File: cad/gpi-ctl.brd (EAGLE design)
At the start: 75 x 73.5 mm, 91 parts, among them CN2 MICROSDPLAIN, CN3 1X4-BIG, IC1 7803SR, SW1 SWITCHGT12-THOLE, SW2 SWITCHKMR211, SW3 SWITCHKMR211, U1 STM32F4/64, U2 ACS711, U3 ULN2003, U8 IC_FT230X-SSOP-16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

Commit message: regulator
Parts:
- removed IC1: 7803SR, adafruit:TO220H
- added C36: (no value), jaw:SMD0603
- added C37: 10u, jaw:SMD0603
- added J4: 1X4-BIG, adafruit:1X04-BIG
- added VREG1: ROF-78E3.3-0.5, jaw:ROF7800
- added VREG2: MCP1824, jaw:SOT-23-5
- moved C3 2.20 mm to (81.4, 29.2)
- moved C1 2.10 mm to (77.9, 29.2)
- moved C7 1.97 mm to (62.0, 59.7)
- moved C27 0.90 mm to (73.5, 62.2)
- moved D1 0.80 mm to (73.4, 60.3)
- moved NY1 0.80 mm to (72.2, 55.7)
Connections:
- new net N$8: D2.C, VREG2.1, VREG2.3
- net GND: now also C36.2, C37.2, J4.2, VREG1.2, VREG2.2; no longer IC1.2
- net I2CC: now also J4.4
- net I2CD: now also J4.3
- net VCC: now also C36.1, C37.1, J4.1, VREG1.3, VREG2.5; no longer IC1.3
- net VCCM: now also VREG1.1; no longer IC1.1
- net VIN: no longer D2.C
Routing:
- net VIN: track 40.8 -> 22.3 mm, vias 0 -> 1
- net N$8: track 0.00 -> 11.7 mm
- net GND: track 149.8 -> 159.6 mm, vias 94 -> 108
- net VCC: track 88.4 -> 96.2 mm, vias 17 -> 21
- net VBUS: track 20.6 -> 26.0 mm, vias 2 -> 3
- net I2CD: track 53.3 -> 58.4 mm, vias 0 -> 1
- net I2CC: track 57.9 -> 60.6 mm
- net VCCM: track 68.6 -> 70.5 mm
- net SPKR: track 35.8 -> 34.1 mm
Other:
- board text added: "C"
- board text added: "D"
- board text added: "T:BT0"
- board text added: "T:G"
- board text added: "T:Rx"
- board text added: "T:Tx"
- board text added: "T:Vi"
- board text added: "T:Vr"
- board text added: "T:Vu"
- board text added: "x"

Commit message: tweak
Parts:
- moved U$1 2.30 mm to (60.5, 44.7)
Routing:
- net SPKR: track 34.1 -> 33.5 mm
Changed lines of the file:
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@@
 <grid distance="0.1" unitdist="mm" unit="mm" style="lines" multiple="10" display="yes" altdistance="0.025" altunitdist="inch" altunit="inch"/>
 <layers>
-<layer number="1" name="Top" color="4" fill="1" visible="no" active="yes"/>
+<layer number="1" name="Top" color="4" fill="1" visible="yes" active="yes"/>
 <layer number="2" name="power" color="5" fill="1" visible="no" active="yes"/>
 <layer number="3" name="Route3" color="4" fill="3" visible="no" active="no"/>
 <layer number="14" name="Route14" color="1" fill="6" visible="no" active="no"/>
 <layer number="15" name="gnd" color="6" fill="1" visible="no" active="yes"/>
-<layer number="16" name="Bottom" color="1" fill="1" visible="no" active="yes"/>
+<layer number="16" name="Bottom" color="1" fill="1" visible="yes" active="yes"/>
 <layer number="17" name="Pads" color="2" fill="1" visible="yes" active="yes"/>
 <layer number="18" name="Vias" color="2" fill="1" visible="yes" active="yes"/>
@@
 <attribute name="VALUE" x="48.986" y="67.622" size="1" layer="27" font="vector" ratio="10" rot="R90"/>
 </element>
-<element name="U$1" library="jaw" package="ROBOTMAN-LOGO" value="ROBOTMAN-LOGO" x="60.5" y="47" rot="R270"/>
+<element name="U$1" library="jaw" package="ROBOTMAN-LOGO" value="ROBOTMAN-LOGO" x="60.5" y="44.7" rot="R270"/>
 <element name="VREG2" library="jaw" package="SOT-23-5" value="MCP1824" x="65.1" y="20.5" smashed="yes">
 <attribute name="NAME" x="63.3125" y="22.3225" size="1" layer="25" font="vector" ratio="10"/>
@@
 <via x="84.1" y="49.3" extent="1-16" drill="0.35"/>
 <via x="71.7" y="49" extent="1-16" drill="0.35"/>
-<via x="64.3" y="49.5" extent="1-16" drill="0.35"/>
+<via x="64" y="50.3" extent="1-16" drill="0.35"/>
 <contactref element="VREG2" pad="2"/>
 <contactref element="C36" pad="2"/>
@@
 <wire x1="61.4" y1="62.9" x2="63" y2="65.6" width="0" layer="19" extent="1-1"/>
 <wire x1="62.6" y1="54.7" x2="63.2" y2="60.5" width="0" layer="19" extent="1-1"/>
-<wire x1="64.3" y1="49.5" x2="62.6" y2="54.7" width="0" layer="19" extent="1-1"/>
+<wire x1="64" y1="50.3" x2="62.6" y2="54.7" width="0" layer="19" extent="1-1"/>
 <wire x1="62" y1="70.2" x2="61.4" y2="62.9" width="0" layer="19" extent="1-1"/>
-<wire x1="71.7" y1="49" x2="64.3" y2="49.5" width="0" layer="19" extent="1-1"/>
+<wire x1="71.7" y1="49" x2="64" y2="50.3" width="0" layer="19" extent="1-1"/>
 <wire x1="75.5" y1="46.9" x2="71.7" y2="49" width="0" layer="19" extent="1-1"/>
 <wire x1="78.3" y1="49.9" x2="75.5" y2="46.9" width="0" layer="19" extent="1-1"/>
@@
 <via x="77.2" y="15.7" extent="1-16" drill="0.35"/>
 <wire x1="77.2" y1="15.7" x2="77.2" y2="17" width="0.35" layer="1"/>
-<wire x1="74.51" y1="60.32" x2="74.51" y2="57.62" width="0.35" layer="1"/>
-<wire x1="74.51" y1="57.62" x2="74.4" y2="57.31" width="0.35" layer="1"/>
-<wire x1="74.51" y1="57.62" x2="77.3" y2="57.62" width="0.35" layer="1"/>
-<wire x1="77.3" y1="57.62" x2="77.92" y2="57.6" width="0.35" layer="1"/>
 <via x="74.3" y="65.4" extent="1-16" drill="0.35"/>
 <wire x1="48.32" y1="9.72" x2="48.32" y2="9.18" width="0.35" layer="1"/>
@@
 <wire x1="62.1" y1="21.8" x2="62.1" y2="23" width="0.5" layer="1"/>
 <contactref element="J4" pad="1"/>
-<wire x1="25.17" y1="10.54" x2="66.7" y2="61.5" width="0" layer="19" extent="1-1"/>
+<wire x1="74.4" y1="57.31" x2="74.69" y2="57.6" width="0.35" layer="1"/>
+<wire x1="74.69" y1="57.6" x2="77.92" y2="57.6" width="0.35" layer="1"/>
+<wire x1="74.51" y1="60.32" x2="74.51" y2="57.42" width="0.35" layer="1"/>
+<wire x1="74.51" y1="57.42" x2="74.4" y2="57.31" width="0.35" layer="1"/>
 </signal>
 <signal name="VCCA">
@@
 <wire x1="66.675" y1="30.175" x2="67.6" y2="31.1" width="0.35" layer="1"/>
 <wire x1="67.6" y1="31.1" x2="67.6" y2="51.2" width="0.35" layer="1"/>
-<wire x1="70" y1="57.31" x2="70.71" y2="57.51" width="0.35" layer="1"/>
-<wire x1="70.71" y1="57.51" x2="72.3" y2="59.1" width="0.35" layer="1"/>
-<wire x1="72.3" y1="59.1" x2="72.3" y2="60.51" width="0.35" layer="1"/>
-<wire x1="72.3" y1="60.51" x2="72.31" y2="60.32" width="0.35" layer="1"/>
 <wire x1="67.6" y1="51.2" x2="70" y2="53.6" width="0.3" layer="1"/>
 <wire x1="70" y1="53.6" x2="70" y2="57.31" width="0.3" layer="1"/>
+<wire x1="72.31" y1="60.32" x2="72.31" y2="59.62" width="0.35" layer="1"/>
+<wire x1="72.31" y1="59.62" x2="70" y2="57.31" width="0.35" layer="1"/>
 </signal>
 <signal name="VCCM">
@@
 <wire x1="64.2" y1="52" x2="65.4" y2="50.8" width="0.3" layer="1"/>
 <wire x1="65.4" y1="50.8" x2="65.4" y2="34.4" width="0.3" layer="1"/>
-<wire x1="66.7" y1="56.42" x2="66.78" y2="56.4" width="0.3" layer="16"/>
-<wire x1="66.78" y1="56.4" x2="63.5" y2="56.4" width="0.3" layer="16"/>
 <via x="63.5" y="56.4" extent="1-16" drill="0.35"/>
 <wire x1="63.5" y1="56.4" x2="64.2" y2="56.4" width="0.3" layer="1"/>
+<wire x1="63.5" y1="56.4" x2="66.68" y2="56.4" width="0.35" layer="16"/>
+<wire x1="66.68" y1="56.4" x2="66.7" y2="56.42" width="0.35" layer="16"/>
 </signal>
 <signal name="ADC5">

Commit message: tweak sent to fab
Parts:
- C36: value (none) -> 10u
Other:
- outline, holes or cut-outs redrawn

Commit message: tweak text
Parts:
- C1: value 10u -> 10u 25V
- LED1: value (none) -> green
- LED2: value (none) -> red
- LED3: value (none) -> white

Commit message: temp sensor
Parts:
- added C38, R15: (no value), jaw:SMD0603
- moved U4 1.00 mm to (50.0, 48.4)
- moved C31 0.92 mm to (53.0, 48.0)
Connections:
- new net N$9: R15.1, U4.2
- net ADCTMP: now also C38.1, R15.2; no longer U4.2
- net GND: now also C38.2
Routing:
- net GND: track 159.6 -> 168.1 mm
- net N$9: track 0.00 -> 2.89 mm
- net ADCTMP: track 16.7 -> 18.8 mm

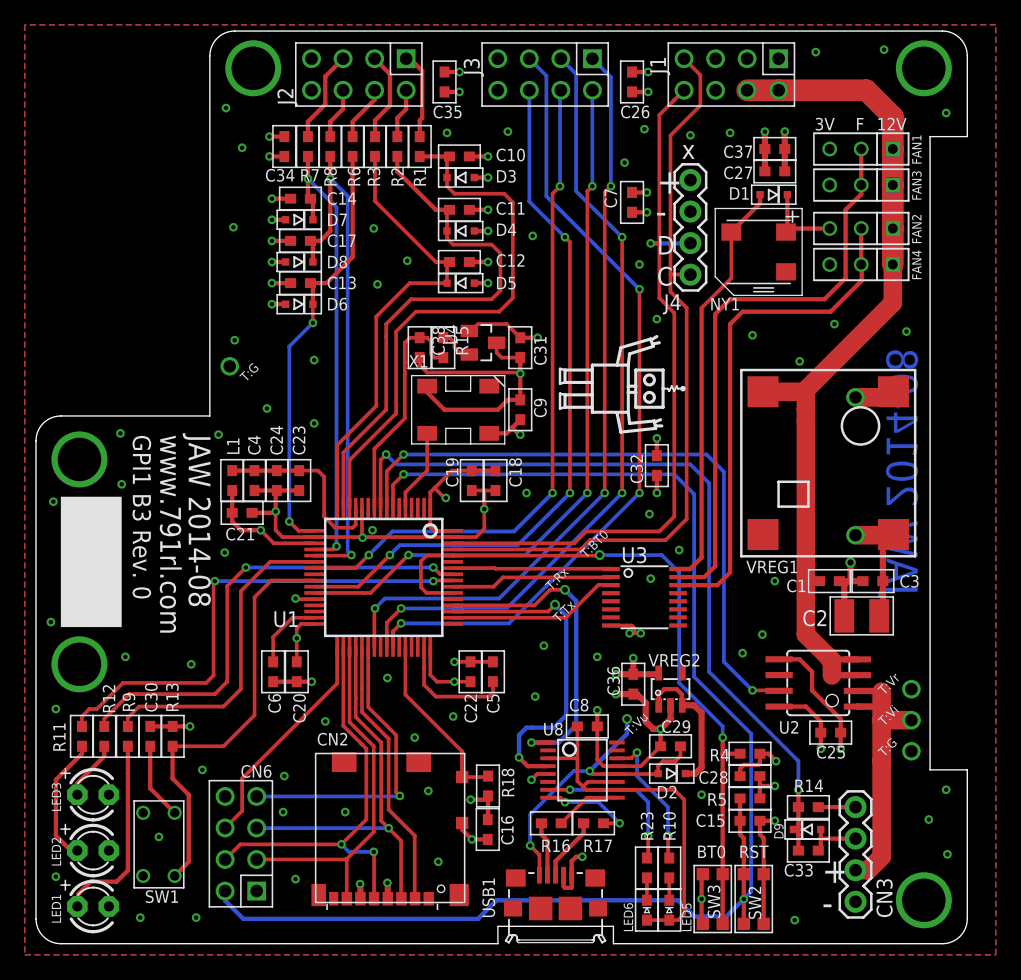
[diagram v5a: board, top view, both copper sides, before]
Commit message: op amp on v-div
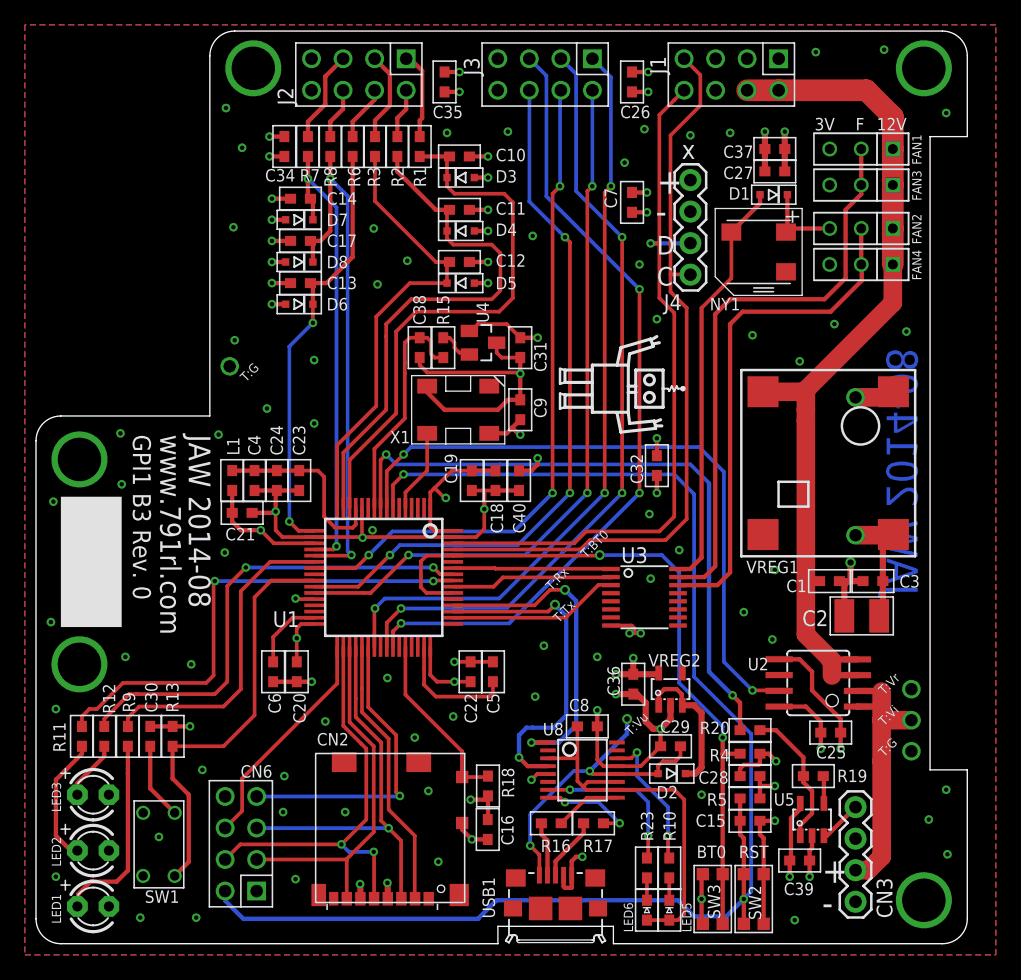
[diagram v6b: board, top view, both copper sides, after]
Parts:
- removed C33: .001u, jaw:SMD0603
- removed D9: 4v, jaw:SOD-323
- removed R14: 100, jaw:SMD0603
- added C39: .1u, jaw:SMD0603
- added C40: 1u, jaw:SMD0603
- added R19: 22, jaw:SMD0603
- added R20: 100, jaw:SMD0603
- added U5: max4452, jaw:SOT-23-5
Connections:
- removed net ADCVIN: CN3.1, R14.2
- new net N$10: R19.1, U5.4
- new net N$11: R19.2, R20.1, U5.1
- new net N$13: CN3.1, U5.3
- net GND: now also C39.2, C40.2, U5.2; no longer C33.2, D9.A
- net IOC1: now also C40.1, R20.2; no longer C33.1, D9.C, R14.1
- net VCC: now also C39.1, U5.5
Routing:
- net N$11: track 0.00 -> 11.4 mm
- net IOC1: track 64.4 -> 55.1 mm, vias 2 -> 3
- net VCC: track 96.3 -> 102.5 mm, vias 21 -> 22
- net N$13: track 0.00 -> 3.50 mm
- net ADCVIN: track 3.00 -> 0.00 mm
- net N$10: track 0.00 -> 2.22 mm
- net GND: track 168.1 -> 168.7 mm

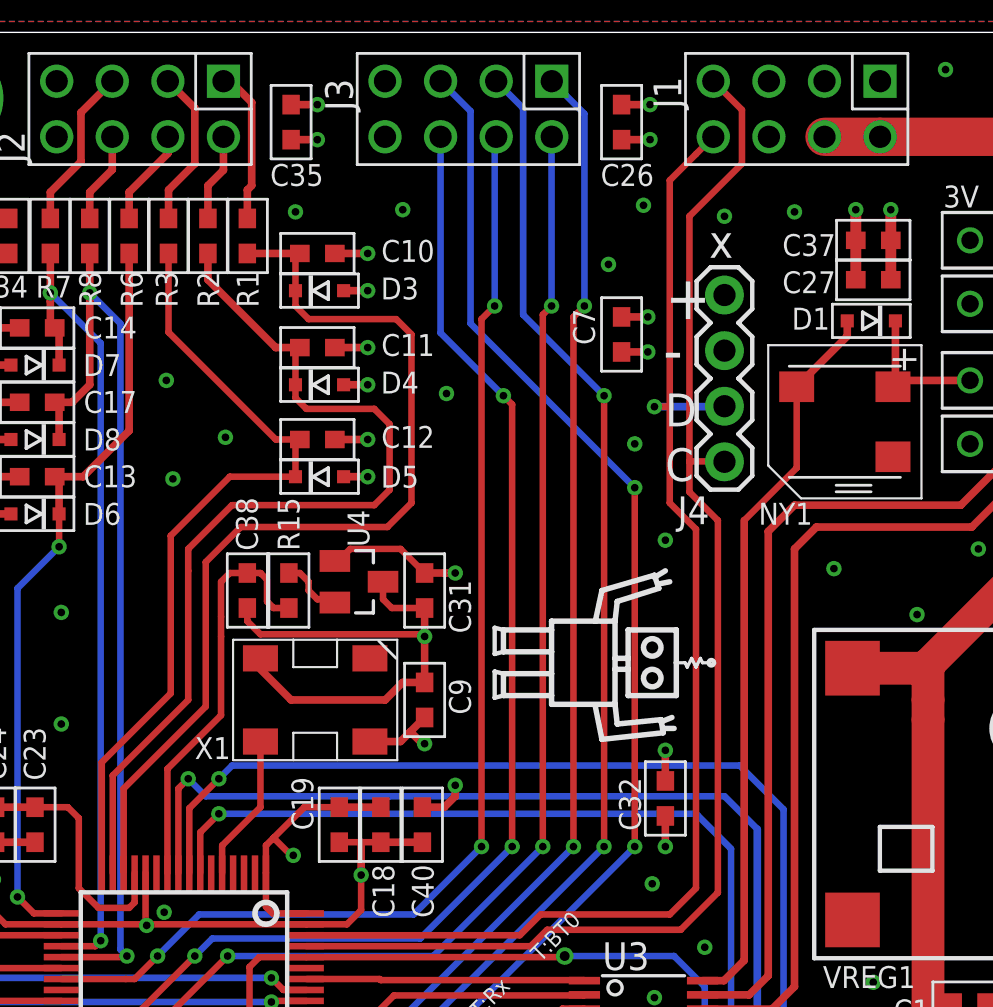
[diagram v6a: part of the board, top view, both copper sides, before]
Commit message: vcca to conn
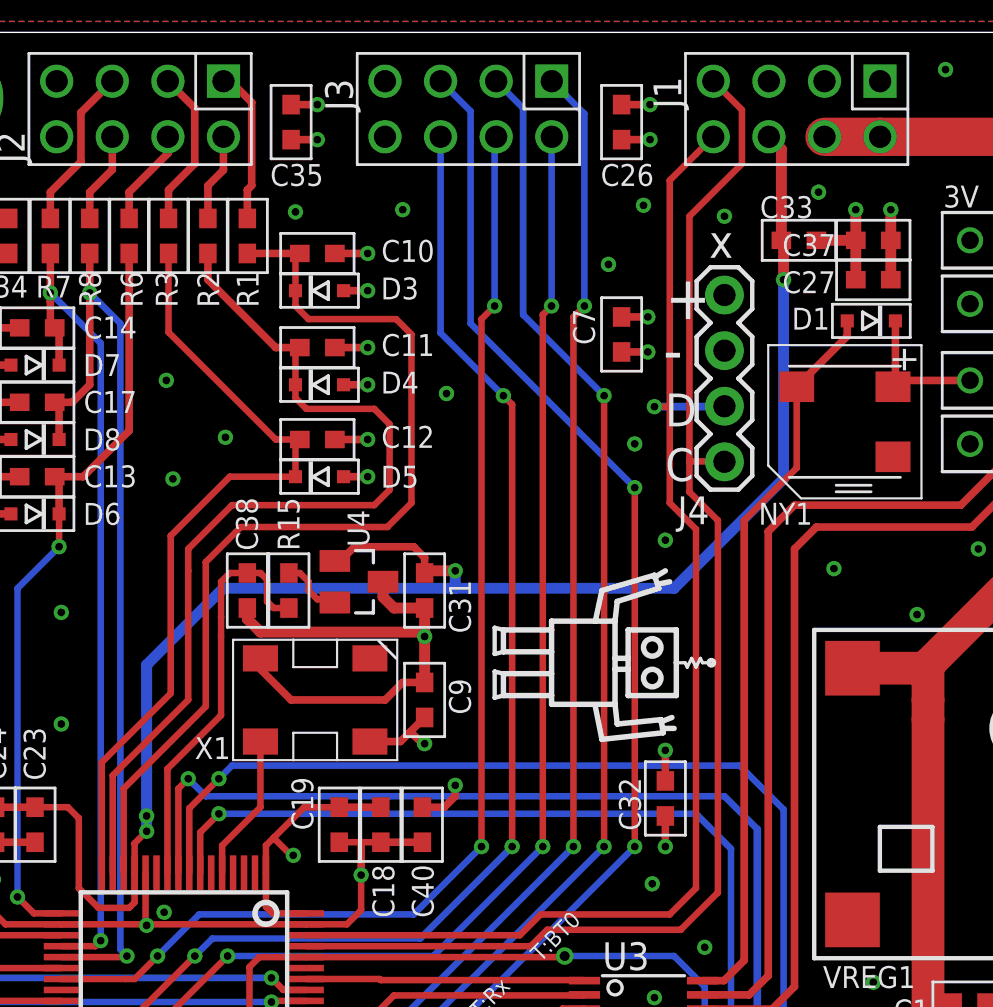
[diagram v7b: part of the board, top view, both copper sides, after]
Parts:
- added C33: 1u, jaw:SMD0603
- C11, C12: value .001u -> .1u
- C13, C14: value .001u -> 1u
- C38: value (none) -> 1u
- C40: value 1u -> .1u
- R15: value (none) -> 100
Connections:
- net GND: now also C33.2
- net VCC: no longer C31.1, J1.6, U4.1
- net VCCA: now also C31.1, C33.1, J1.6, U4.1
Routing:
- net VCCA: track 15.2 -> 81.0 mm, vias 0 -> 4
- net VCC: track 102.5 -> 96.3 mm, vias 22 -> 21
- net GND: track 168.7 -> 170.5 mm

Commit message: sync, green led
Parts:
- added CN1: HEADER-1X2.4, jaw:HEADER-1X2-THM-WIDE
- R9: value 1k -> 470
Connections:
- new net N$12: CN1.2, U1.22
- net GND: now also CN1.1
- net IOLED1: now also U1.40; no longer U1.22
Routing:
- net N$12: track 0.00 -> 20.9 mm
- net IOLED1: track 25.5 -> 24.9 mm, vias 0 -> 2
- net GND: vias 108 -> 107
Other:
- board text added: "T:Sync"
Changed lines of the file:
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@@
 <text x="56.1" y="25.8" size="0.75" layer="21" ratio="10" rot="R45">T:Tx</text>
 <text x="58.3" y="31" size="0.75" layer="21" ratio="10" rot="R45">T:BT0</text>
-<text x="30.9" y="45.2" size="0.75" layer="21" ratio="10" rot="R45">T:G</text>
+<text x="31.4" y="49.3" size="0.75" layer="21" ratio="10" rot="R45">T:G</text>
 <text x="61.9" y="16.7" size="0.75" layer="21" ratio="10" rot="R45">T:Vu</text>
 <text x="64" y="60.4" size="2" layer="21" ratio="15">+</text>
@@
 <text x="64" y="53" size="1.5" layer="21" ratio="15">C</text>
 <text x="66" y="63.2" size="1.5" layer="21" ratio="15">x</text>
+<text x="31.4" y="43.2" size="0.75" layer="21" ratio="10" rot="R45">T:Sync</text>
 </plain>
 <attributes>
@@
 <attribute name="NAME" x="48.4575" y="71.38" size="1.27" layer="25" font="vector" ratio="10" rot="R270"/>
 </element>
-<element name="R9" library="jaw" package="SMD0603" value="1k" x="21.4" y="16.7" smashed="yes" rot="R90">
+<element name="R9" library="jaw" package="SMD0603" value="470" x="21.4" y="16.7" smashed="yes" rot="R90">
 <attribute name="NAME" x="21.984" y="18.622" size="1" layer="25" font="vector" ratio="10" rot="R90"/>
 <attribute name="VALUE" x="21.786" y="19.022" size="1" layer="27" font="vector" ratio="10" rot="R90"/>
@@
 </element>
 <element name="C33" library="jaw" package="SMD0603" value="1u" x="70.1" y="64"/>
+<element name="CN1" library="jaw" package="HEADER-1X2-THM-WIDE" value="HEADER-1X2.4" x="29.5" y="47.5" rot="R270"/>
 </elements>
 <signals>
@@
 <via x="21.2" y="23.1" extent="1-16" drill="0.35"/>
 <via x="15.6" y="18.9" extent="1-16" drill="0.35"/>
-<via x="29.2" y="31.5" extent="1-16" drill="0.35"/>
-<via x="32.6" y="43.1" extent="1-16" drill="0.35"/>
+<via x="28.9" y="31" extent="1-16" drill="0.35"/>
+<via x="32.7" y="42.3" extent="1-16" drill="0.35"/>
 <via x="36.4" y="41.9" extent="1-16" drill="0.35"/>
 <via x="36.4" y="47" extent="1-16" drill="0.35"/>
 <via x="41.5" y="53.1" extent="1-16" drill="0.35"/>
-<via x="42.3" y="21.4" extent="1-16" drill="0.35"/>
+<via x="42.4" y="20" extent="1-16" drill="0.35"/>
 <via x="47.6" y="18.3" extent="1-16" drill="0.35"/>
 <via x="44.5" y="16.6" extent="1-16" drill="0.35"/>
@@
 <via x="75.1" y="1.9" extent="1-16" drill="0.35"/>
 <via x="20.8" y="41.1" extent="1-16" drill="0.35"/>
-<via x="28.7" y="41" extent="1-16" drill="0.35"/>
+<via x="28.4" y="41" extent="1-16" drill="0.35"/>
 <via x="26.5" y="22.5" extent="1-16" drill="0.35"/>
 <via x="63.4" y="34.6" extent="1-16" drill="0.35"/>
@@
 <via x="45.6" y="12.3" extent="1-16" drill="0.35"/>
 <via x="87.4" y="7.2" extent="1-16" drill="0.35"/>
-<via x="30" y="48.6" extent="1-16" drill="0.35"/>
+<via x="29.8" y="52.2" extent="1-16" drill="0.35"/>
 <via x="30.6" y="64.1" extent="1-16" drill="0.35"/>
 <via x="29.9" y="57.7" extent="1-16" drill="0.35"/>
@@
 <via x="79.6" y="30.7" extent="1-16" drill="0.5"/>
 <wire x1="79.6" y1="30.7" x2="79.6" y2="29.2" width="0.5" layer="1"/>
-<via x="29.6" y="46.5" extent="1-16" drill="1"/>
 <wire x1="72.3" y1="15.3" x2="73" y2="15.3" width="0.35" layer="1"/>
 <wire x1="73" y1="15.3" x2="73.6" y2="14.7" width="0.35" layer="1"/>
@@
 <wire x1="44.9" y1="47.2" x2="44.9" y2="46.7" width="0.5" layer="1"/>
 <wire x1="44.9" y1="46.7" x2="45.5" y2="46.1" width="0.5" layer="1"/>
+<contactref element="CN1" pad="1"/>
 </signal>
 <signal name="VCC">
@@
 <signal name="IOLED1">
 <contactref element="R9" pad="2"/>
-<contactref element="U1" pad="22"/>
-<wire x1="36.4" y1="30.75" x2="32.85" y2="30.75" width="0.3" layer="1"/>
 <wire x1="21.4" y1="17.7" x2="21.4" y2="17.5" width="0.3" layer="1"/>
 <wire x1="21.4" y1="17.7" x2="21.4" y2="18.2" width="0.3" layer="1"/>
 <wire x1="21.4" y1="18.2" x2="22.3" y2="19.1" width="0.3" layer="1"/>
-<wire x1="22.3" y1="19.1" x2="29.1" y2="19.1" width="0.3" layer="1"/>
-<wire x1="29.1" y1="19.1" x2="30.5" y2="20.5" width="0.3" layer="1"/>
-<wire x1="30.5" y1="20.5" x2="30.5" y2="28.4" width="0.3" layer="1"/>
-<wire x1="30.5" y1="28.4" x2="32.85" y2="30.75" width="0.3" layer="1"/>
+<wire x1="22.3" y1="19.1" x2="28.9" y2="19.1" width="0.3" layer="1"/>
+<wire x1="28.9" y1="19.1" x2="29.1" y2="19.1" width="0.3" layer="1"/>
+<wire x1="29.1" y1="19.1" x2="30.5" y2="20.5" width="0" layer="19" extent="1-16"/>
+<wire x1="30.5" y1="20.5" x2="30.5" y2="28.4" width="0" layer="19" extent="1-16"/>
+<wire x1="30.5" y1="28.4" x2="32.85" y2="30.75" width="0" layer="19" extent="1-16"/>
+<contactref element="U1" pad="40"/>
+<wire x1="41.75" y1="23.9" x2="41.75" y2="22.15" width="0.3" layer="1"/>
+<wire x1="41.75" y1="22.15" x2="41.8" y2="22.1" width="0.3" layer="1"/>
+<via x="41.8" y="22.1" extent="1-16" drill="0.35"/>
+<wire x1="41.8" y1="22.1" x2="38.8" y2="19.1" width="0.3" layer="16"/>
+<wire x1="38.8" y1="19.1" x2="28.9" y2="19.1" width="0.3" layer="16"/>
+<via x="28.9" y="19.1" extent="1-16" drill="0.35"/>
+<wire x1="28.9" y1="19.1" x2="29.1" y2="19.1" width="0.3" layer="1"/>
 </signal>
 <signal name="IOLED2">
@@
 <wire x1="77.7" y1="8.7" x2="80" y2="11" width="0.35" layer="1"/>
 </signal>
+<signal name="N$12">
+<contactref element="U1" pad="22"/>
+<contactref element="CN1" pad="2"/>
+<wire x1="36.4" y1="30.75" x2="34.45" y2="30.75" width="0.3" layer="1"/>
+<wire x1="34.45" y1="30.75" x2="33.8" y2="31.4" width="0.3" layer="1"/>
+<wire x1="33.8" y1="31.4" x2="30.8" y2="31.4" width="0.3" layer="1"/>
+<wire x1="30.8" y1="31.4" x2="28.4" y2="33.8" width="0.3" layer="1"/>
+<wire x1="28.4" y1="33.8" x2="28.4" y2="39.1" width="0.3" layer="1"/>
+<wire x1="28.4" y1="39.1" x2="29.5" y2="40.2" width="0.3" layer="1"/>
+<wire x1="29.5" y1="40.2" x2="29.5" y2="44.96" width="0.3" layer="1"/>
+</signal>
 </signals>
